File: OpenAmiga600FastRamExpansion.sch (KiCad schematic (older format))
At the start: 27 parts, among them J1 MC68000_PLCC68, P1 JTAG_CONNECTOR, P99 OSHW_LOGO, U1 74LS157, U2 74LS157, U3 HYB5118160BSJ, U4 HYB5118160BSJ, U5 ATF1502AS-10JU44

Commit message: Ready for routing!
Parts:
- added P98: SCREW_HOLE, MountingHole:MountingHole_2.5mm, symbol conn:CONN_1
- C13, C14: footprint Capacitor_SMD:C_0805_2012Metric_Pad1.15x1.40mm_HandSolder -> Capacitor_SMD:CP_Elec_5x5.8
- J1: footprint Package_LCC:PLCC-68_THT-Socket -> OpenAmiga600FastRamExpansion:PLCC-68_THT-SocketUpsideDown
- LD1: footprint LED_SMD:LED_0805_2012Metric_Pad1.15x1.40mm_HandSolder -> OpenAmiga600FastRamExpansion:LED_0805_HandSoldering_ModSilkS
- U1, U2: footprint Package_SO:SOIC-16W_5.3x10.2mm_P1.27mm -> Package_SO:SOIC-16_3.9x9.9mm_P1.27mm
- U3, U4: footprint OpenAmiga600FastRamExpansion:SOJ-42-Socket-LongPads -> OpenAmiga600FastRamExpansion:SOJ-42-LongPads
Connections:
- no-connect marks 33 -> 34
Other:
- moved on the sheet: C3, C4, C5, C6, C7, C8

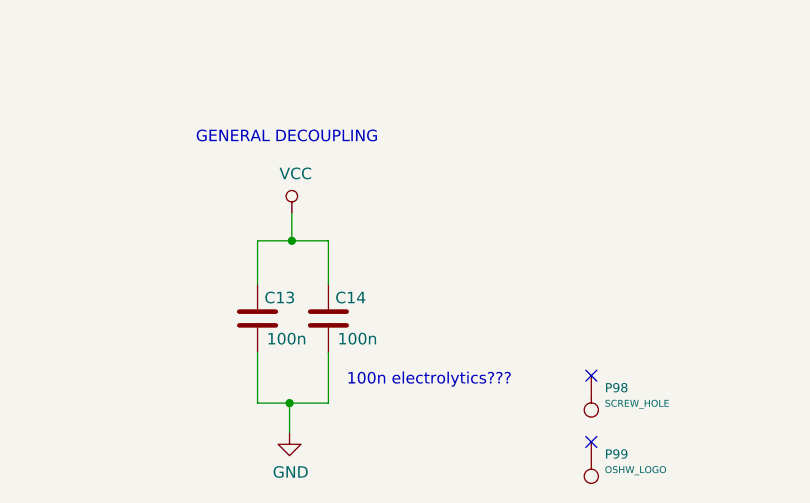
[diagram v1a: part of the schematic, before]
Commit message: Make C13 THT and remove C14
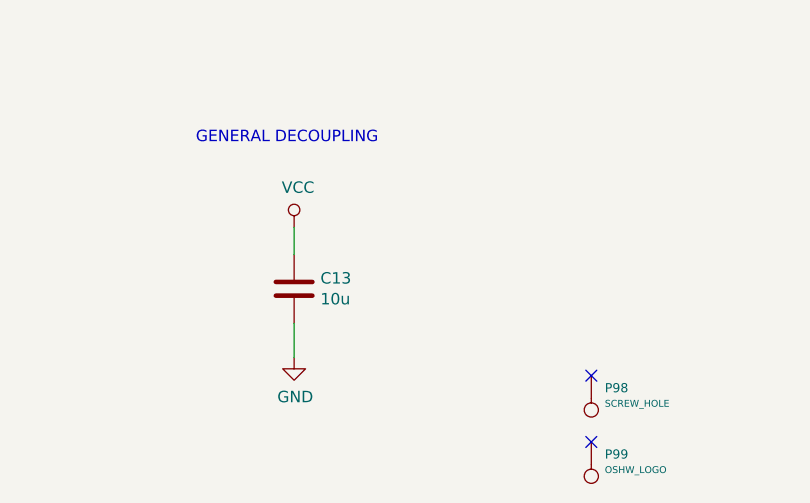
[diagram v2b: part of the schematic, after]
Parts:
- removed C14: 100n, Capacitor_SMD:CP_Elec_5x5.8, symbol Device:C
- C13: value 100n -> 10u; footprint Capacitor_SMD:CP_Elec_5x5.8 -> Capacitor_THT:CP_Radial_D5.0mm_P2.00mm
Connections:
- wire segments 356 -> 348
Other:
- note removed: "100n electrolytics???"
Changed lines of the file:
@@
 Sheet 1 1
 Title "OpenAmiga600FastRamExpansion"
-Date "2019-02-18"
+Date "2019-02-19"
 Rev "1git"
 Comp "SukkoPera"
-Comment1 "Thanks to lvd"
-Comment2 ""
-Comment3 ""
+Comment1 "Based on work by Kipper2K"
+Comment2 "Original design by lvd/NedoPC"
+Comment3 "Licensed under CERN OHL v.1.2"
 Comment4 ""
 $EndDescr
@@
 Text Notes 15430 3530 1    50   ~ 0
 C13 on Kipper2K's board
-$Comp
-L Device:C C13
-U 1 1 5CAED17C
-P 9870 10370
-F 0 "C13" H 9900 10460 50  0000 L CNN
-F 1 "100n" H 9910 10280 50  0000 L CNN
-F 2 "Capacitor_SMD:CP_Elec_5x5.8" H 9908 10220 50  0001 C CNN
-F 3 "~" H 9870 10370 50  0001 C CNN
-	1    9870 10370
-	1    0    0    -1
-$EndComp
-$Comp
-L Device:C C14
-U 1 1 5CAED183
-P 10180 10370
-F 0 "C14" H 10210 10460 50  0000 L CNN
-F 1 "100n" H 10220 10280 50  0000 L CNN
-F 2 "Capacitor_SMD:CP_Elec_5x5.8" H 10218 10220 50  0001 C CNN
-F 3 "~" H 10180 10370 50  0001 C CNN
-	1    10180 10370
-	1    0    0    -1
-$EndComp
-Wire Wire Line
-	10180 10030 10180 10220
-Connection ~ 10020 10030
-Wire Wire Line
-	10020 10030 10180 10030
-$Comp
-L power:VCC #PWR027
-U 1 1 5CAED18F
-P 10020 9910
-F 0 "#PWR027" H 10020 9760 50  0001 C CNN
-F 1 "VCC" H 10037 10083 50  0000 C CNN
-F 2 "" H 10020 9910 50  0001 C CNN
-F 3 "" H 10020 9910 50  0001 C CNN
-	1    10020 9910
-	1    0    0    -1
-$EndComp
-Wire Wire Line
-	10020 9910 10020 10030
-$Comp
-L power:GND #PWR026
-U 1 1 5CAED196
-P 10010 10870
-F 0 "#PWR026" H 10010 10620 50  0001 C CNN
-F 1 "GND" H 10015 10697 50  0000 C CNN
-F 2 "" H 10010 10870 50  0001 C CNN
-F 3 "" H 10010 10870 50  0001 C CNN
-	1    10010 10870
-	1    0    0    -1
-$EndComp
-Wire Wire Line
-	10180 10740 10180 10520
-Wire Wire Line
-	9870 10520 9870 10740
-Wire Wire Line
-	9870 10740 10010 10740
-Wire Wire Line
-	9870 10220 9870 10030
-Wire Wire Line
-	9870 10030 10020 10030
-Wire Wire Line
-	10010 10870 10010 10740
-Connection ~ 10010 10740
-Wire Wire Line
-	10010 10740 10180 10740
 Text Notes 9600 9610 0    50   ~ 0
 GENERAL DECOUPLING
-Text Notes 10260 10670 0    50   ~ 0
-100n electrolytics???
 $Comp
 L power:VCC #PWR030
@@
 $EndComp
 NoConn ~ 11330 10620
+$Comp
+L Device:C C13
+U 1 1 5CD6434E
+P 10030 10240
+F 0 "C13" H 10145 10286 50  0000 L CNN
+F 1 "10u" H 10145 10195 50  0000 L CNN
+F 2 "Capacitor_THT:CP_Radial_D5.0mm_P2.00mm" H 10068 10090 50  0001 C CNN
+F 3 "~" H 10030 10240 50  0001 C CNN
+	1    10030 10240
+	1    0    0    -1
+$EndComp
+$Comp
+L power:VCC #PWR0105
+U 1 1 5CD64354
+P 10030 9970
+F 0 "#PWR0105" H 10030 9820 50  0001 C CNN
+F 1 "VCC" H 10047 10143 50  0000 C CNN
+F 2 "" H 10030 9970 50  0001 C CNN
+F 3 "" H 10030 9970 50  0001 C CNN
+	1    10030 9970
+	1    0    0    -1
+$EndComp
+$Comp
+L power:GND #PWR0106
+U 1 1 5CD6435A
+P 10030 10540
+F 0 "#PWR0106" H 10030 10290 50  0001 C CNN
+F 1 "GND" H 10035 10367 50  0000 C CNN
+F 2 "" H 10030 10540 50  0001 C CNN
+F 3 "" H 10030 10540 50  0001 C CNN
+	1    10030 10540
+	1    0    0    -1
+$EndComp
+Wire Wire Line
+	10030 9970 10030 10090
+Wire Wire Line
+	10030 10390 10030 10540
 Wire Bus Line
 	11610 4190 11610 8500

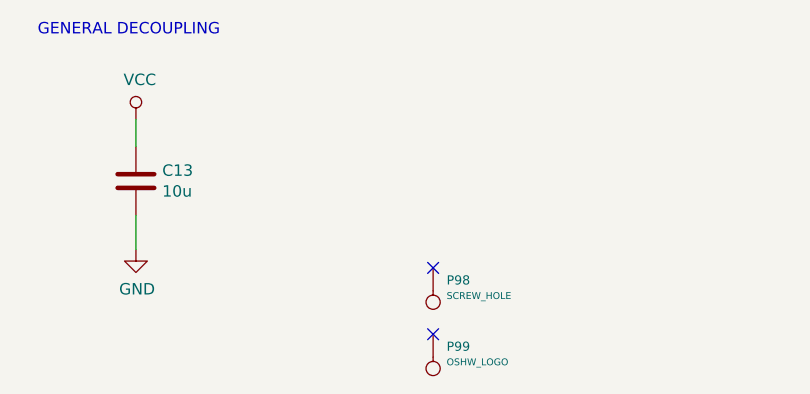
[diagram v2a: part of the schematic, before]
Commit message: Connect screw hole to ground plate
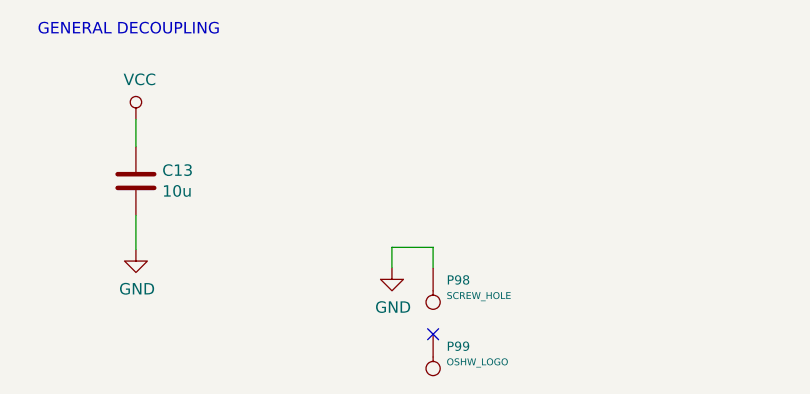
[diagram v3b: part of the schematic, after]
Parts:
- P98: footprint MountingHole:MountingHole_2.5mm -> MountingHole:MountingHole_2.5mm_Pad_Via
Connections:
- wire segments 348 -> 351
- no-connect marks 34 -> 33
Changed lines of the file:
@@
 Sheet 1 1
 Title "OpenAmiga600FastRamExpansion"
-Date "2019-02-19"
+Date "2019-02-27"
 Rev "1git"
 Comp "SukkoPera"
@@
 F 0 "P98" V 11234 10829 40  0000 L CNN
 F 1 "SCREW_HOLE" V 11302 10829 30  0000 L CNN
-F 2 "MountingHole:MountingHole_2.5mm" H 11330 10770 50  0001 C CNN
+F 2 "MountingHole:MountingHole_2.5mm_Pad_Via" H 11330 10770 50  0001 C CNN
 F 3 "" H 11330 10770 50  0001 C CNN
 	1    11330 10770
 	0    1    1    0
 $EndComp
-NoConn ~ 11330 10620
 $Comp
 L Device:C C13
@@
 Wire Wire Line
 	10030 10390 10030 10540
+$Comp
+L power:GND #PWR0107
+U 1 1 5CE962C3
+P 11150 10620
+F 0 "#PWR0107" H 11150 10370 50  0001 C CNN
+F 1 "GND" H 11155 10447 50  0000 C CNN
+F 2 "" H 11150 10620 50  0001 C CNN
+F 3 "" H 11150 10620 50  0001 C CNN
+	1    11150 10620
+	1    0    0    -1
+$EndComp
+Wire Wire Line
+	11150 10620 11150 10530
+Wire Wire Line
+	11150 10530 11330 10530
+Wire Wire Line
+	11330 10530 11330 10620
 Wire Bus Line
 	11610 4190 11610 8500

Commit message: Use real IDC-10 connector for JTAG
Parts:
- P1: footprint Connector_PinHeader_2.54mm:PinHeader_2x05_P2.54mm_Vertical -> Connector_IDC:IDC-Header_2x05_P2.54mm_Vertical
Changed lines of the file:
@@
 F 0 "P1" H 7780 10893 60  0000 C CNN
 F 1 "JTAG_CONNECTOR" H 7780 10795 50  0000 C CNN
-F 2 "Connector_PinHeader_2.54mm:PinHeader_2x05_P2.54mm_Vertical" H 7780 10450 50  0001 C CNN
+F 2 "Connector_IDC:IDC-Header_2x05_P2.54mm_Vertical" H 7780 10450 50  0001 C CNN
 F 3 "" H 7780 10450 50  0001 C CNN
 	1    7780 10450
